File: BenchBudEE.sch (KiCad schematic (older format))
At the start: 0 parts

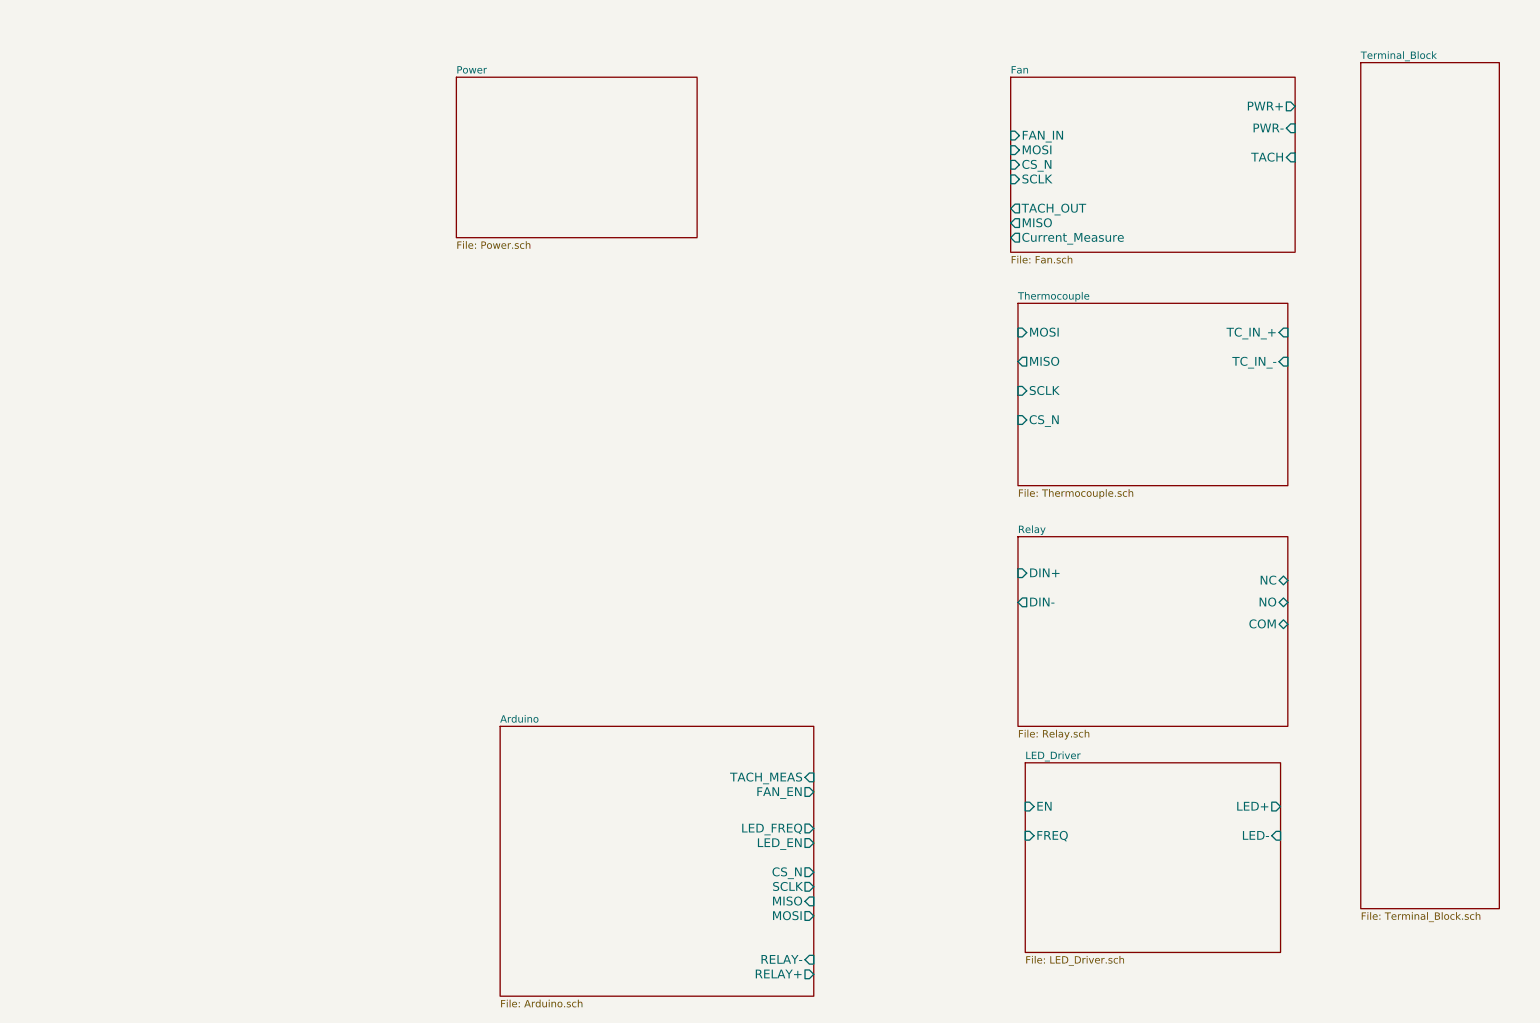
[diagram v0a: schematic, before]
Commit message: Created the first schematic in both Power modules
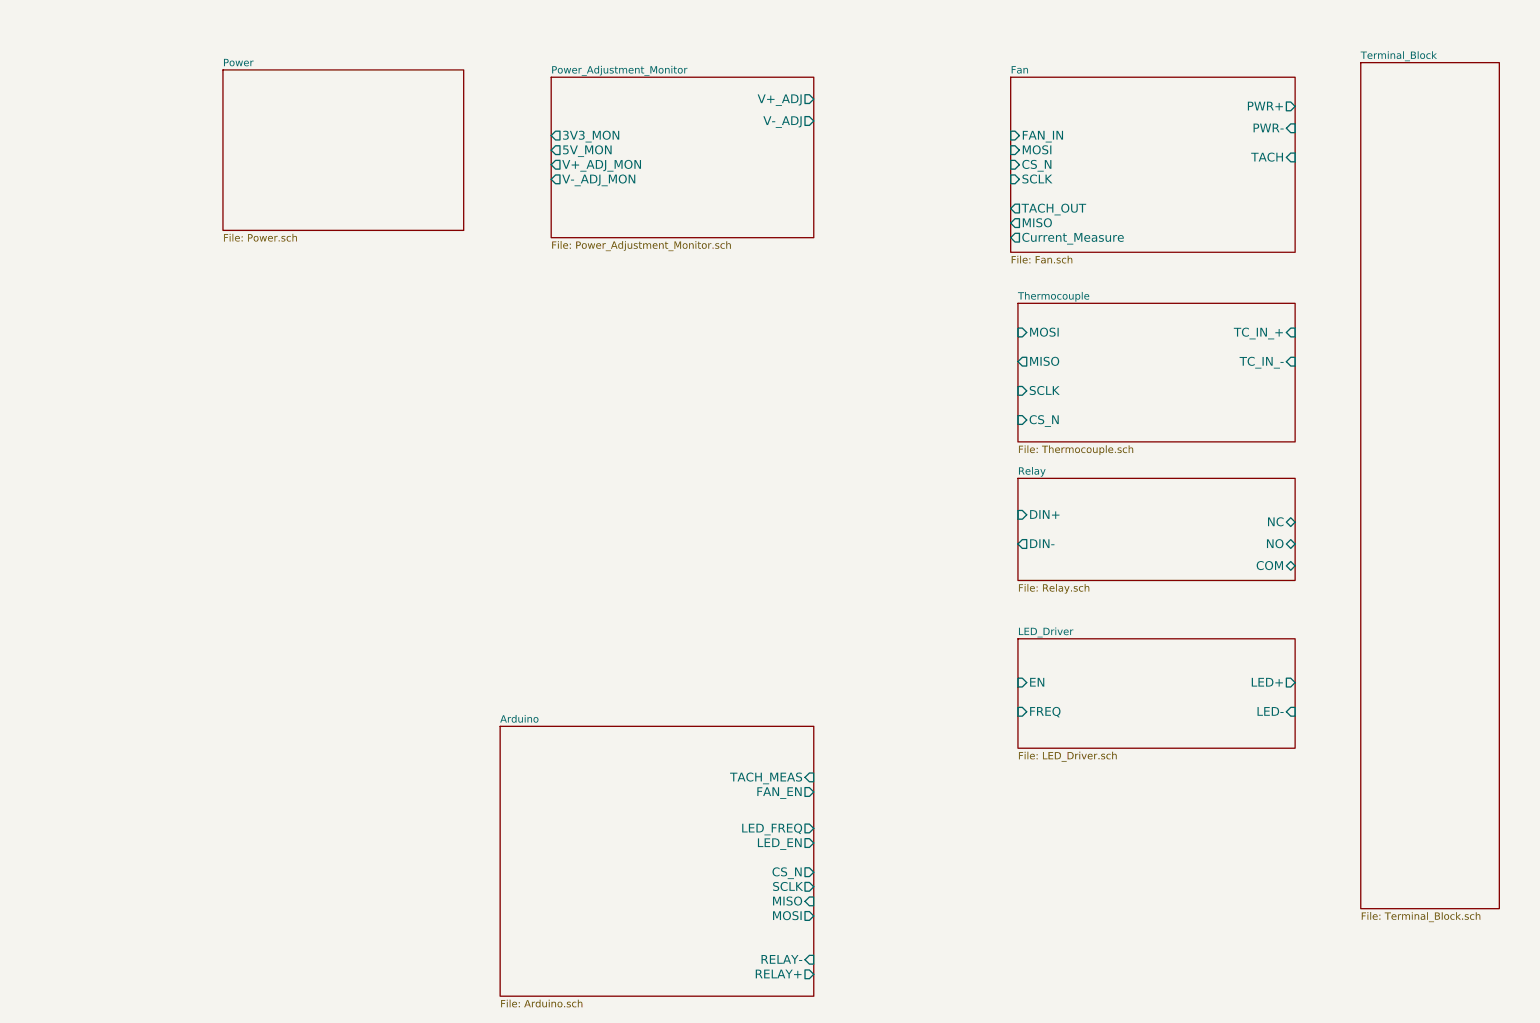
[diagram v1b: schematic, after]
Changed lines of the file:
@@
 $Descr A4 11693 8268
 encoding utf-8
-Sheet 1 8
+Sheet 1 9
 Title ""
-Date "9 feb 2014"
+Date "10 feb 2014"
 Rev ""
 Comp ""
@@
 $EndSheet
 $Sheet
-S 7550 2550 1850 1250
+S 7550 2550 1900 950
 U 52EE0AFF
 F0 "Thermocouple" 50
 F1 "Thermocouple.sch" 50
-F2 "TC_IN_+" I R 9400 2750 60
-F3 "TC_IN_-" I R 9400 2950 60
+F2 "TC_IN_+" I R 9450 2750 60
+F3 "TC_IN_-" I R 9450 2950 60
 F4 "MOSI" I L 7550 2750 60
 F5 "MISO" O L 7550 2950 60
@@
 $EndSheet
 $Sheet
-S 3700 1000 1650 1100
+S 2100 950  1650 1100
 U 52EE0B23
 F0 "Power" 50
@@
 $EndSheet
 $Sheet
-S 7600 5700 1750 1300
+S 7550 4850 1900 750
 U 52EE0B45
 F0 "LED_Driver" 50
 F1 "LED_Driver.sch" 50
-F2 "EN" I L 7600 6000 60
-F3 "FREQ" I L 7600 6200 60
-F4 "LED+" O R 9350 6000 60
-F5 "LED-" I R 9350 6200 60
+F2 "EN" I L 7550 5150 60
+F3 "FREQ" I L 7550 5350 60
+F4 "LED+" O R 9450 5150 60
+F5 "LED-" I R 9450 5350 60
 $EndSheet
 $Sheet
@@
 $EndSheet
 $Sheet
-S 7550 4150 1850 1300
+S 7550 3750 1900 700
 U 52EE0B15
 F0 "Relay" 50
 F1 "Relay.sch" 50
-F2 "DIN+" I L 7550 4400 60
-F3 "DIN-" O L 7550 4600 60
-F4 "NC" B R 9400 4450 60
-F5 "NO" B R 9400 4600 60
-F6 "COM" B R 9400 4750 60
+F2 "DIN+" I L 7550 4000 60
+F3 "DIN-" O L 7550 4200 60
+F4 "NC" B R 9450 4050 60
+F5 "NO" B R 9450 4200 60
+F6 "COM" B R 9450 4350 60
+$EndSheet
+$Sheet
+S 4350 1000 1800 1100
+U 52F76568
+F0 "Power_Adjustment_Monitor" 50
+F1 "Power_Adjustment_Monitor.sch" 50
+F2 "V+_ADJ" O R 6150 1150 60
+F3 "V-_ADJ" O R 6150 1300 60
+F4 "3V3_MON" O L 4350 1400 60
+F5 "5V_MON" O L 4350 1500 60
+F6 "V+_ADJ_MON" O L 4350 1600 60
+F7 "V-_ADJ_MON" O L 4350 1700 60
 $EndSheet
 $EndSCHEMATC

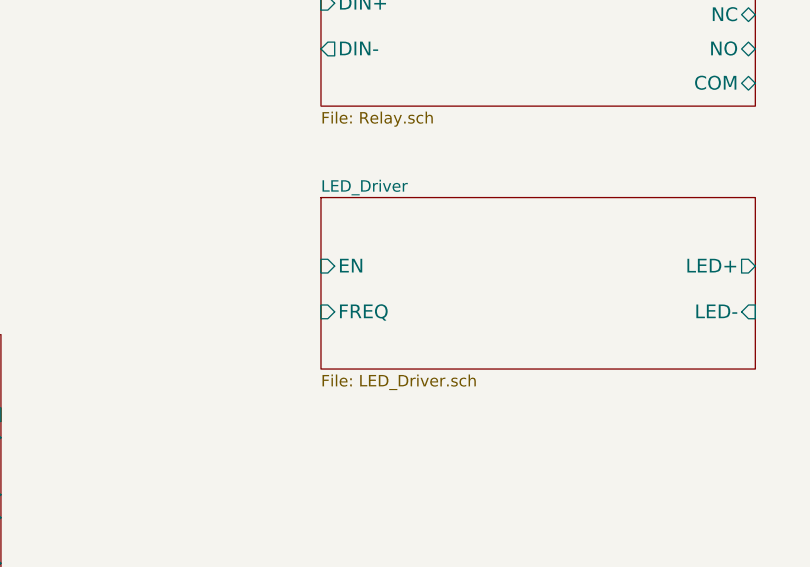
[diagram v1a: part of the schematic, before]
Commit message: Created first schematic for LED module
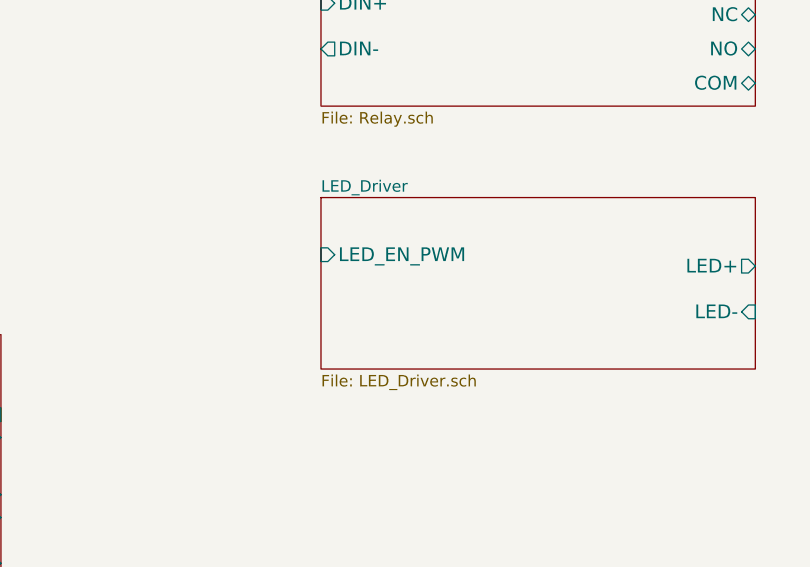
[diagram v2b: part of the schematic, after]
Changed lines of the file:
@@
 F0 "LED_Driver" 50
 F1 "LED_Driver.sch" 50
-F2 "EN" I L 7550 5150 60
-F3 "FREQ" I L 7550 5350 60
-F4 "LED+" O R 9450 5150 60
-F5 "LED-" I R 9450 5350 60
+F2 "LED+" O R 9450 5150 60
+F3 "LED-" I R 9450 5350 60
+F4 "LED_EN_PWM" I L 7550 5100 60
 $EndSheet
 $Sheet

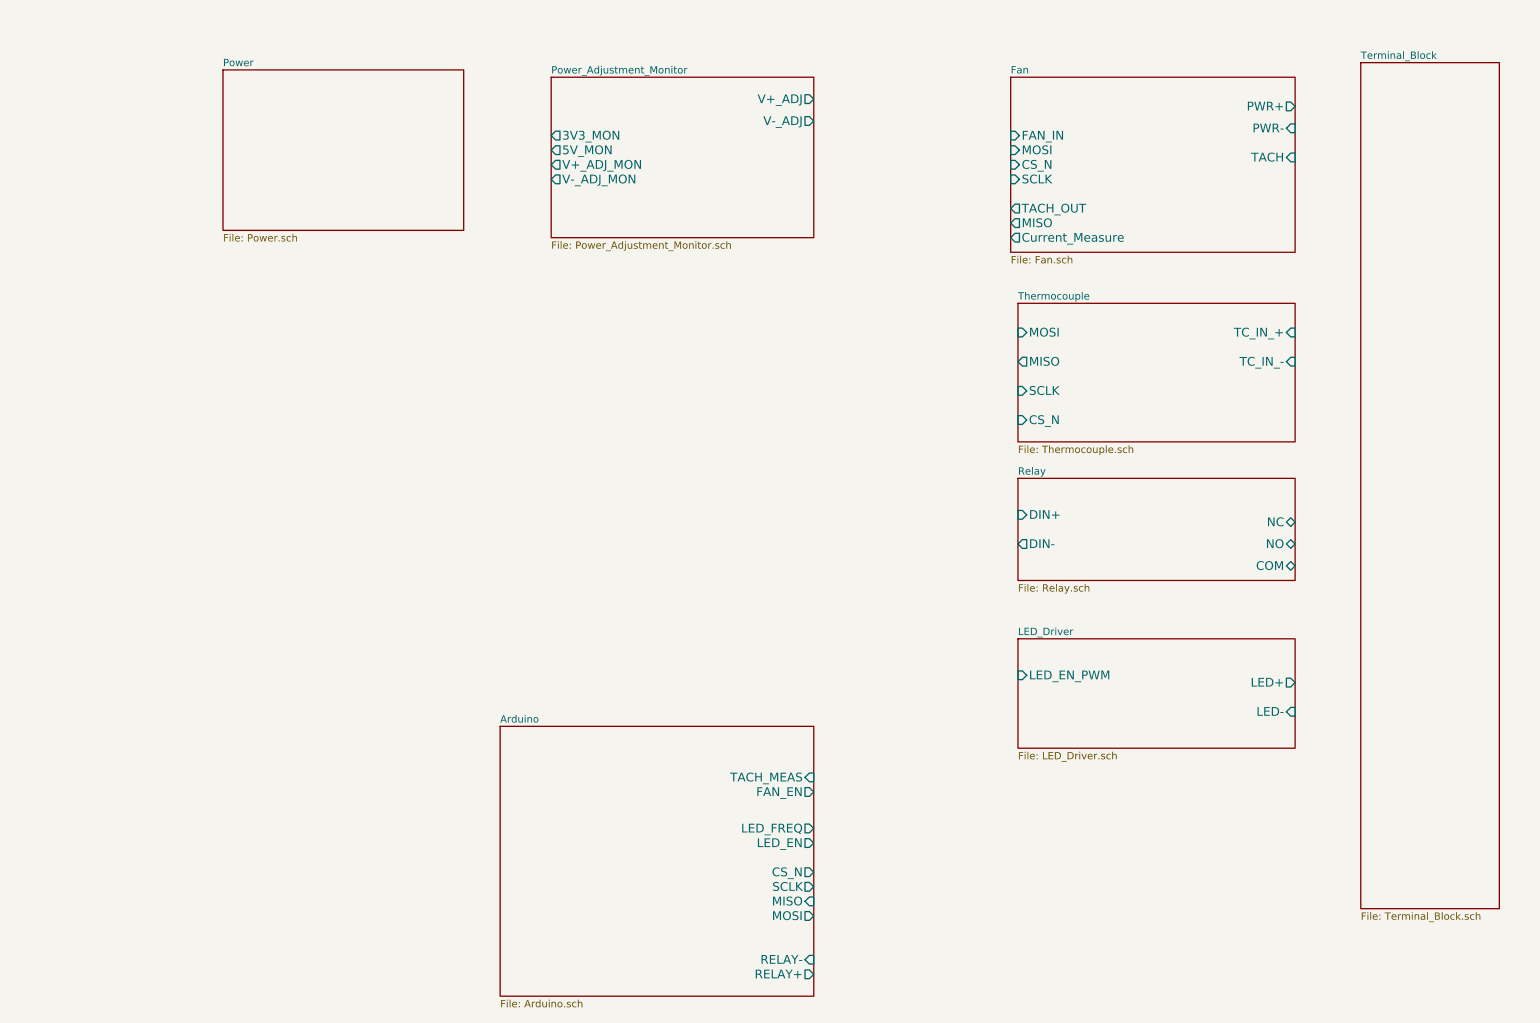
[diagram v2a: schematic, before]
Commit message: Created the Arduino module and then connected all the modules in the main schematic
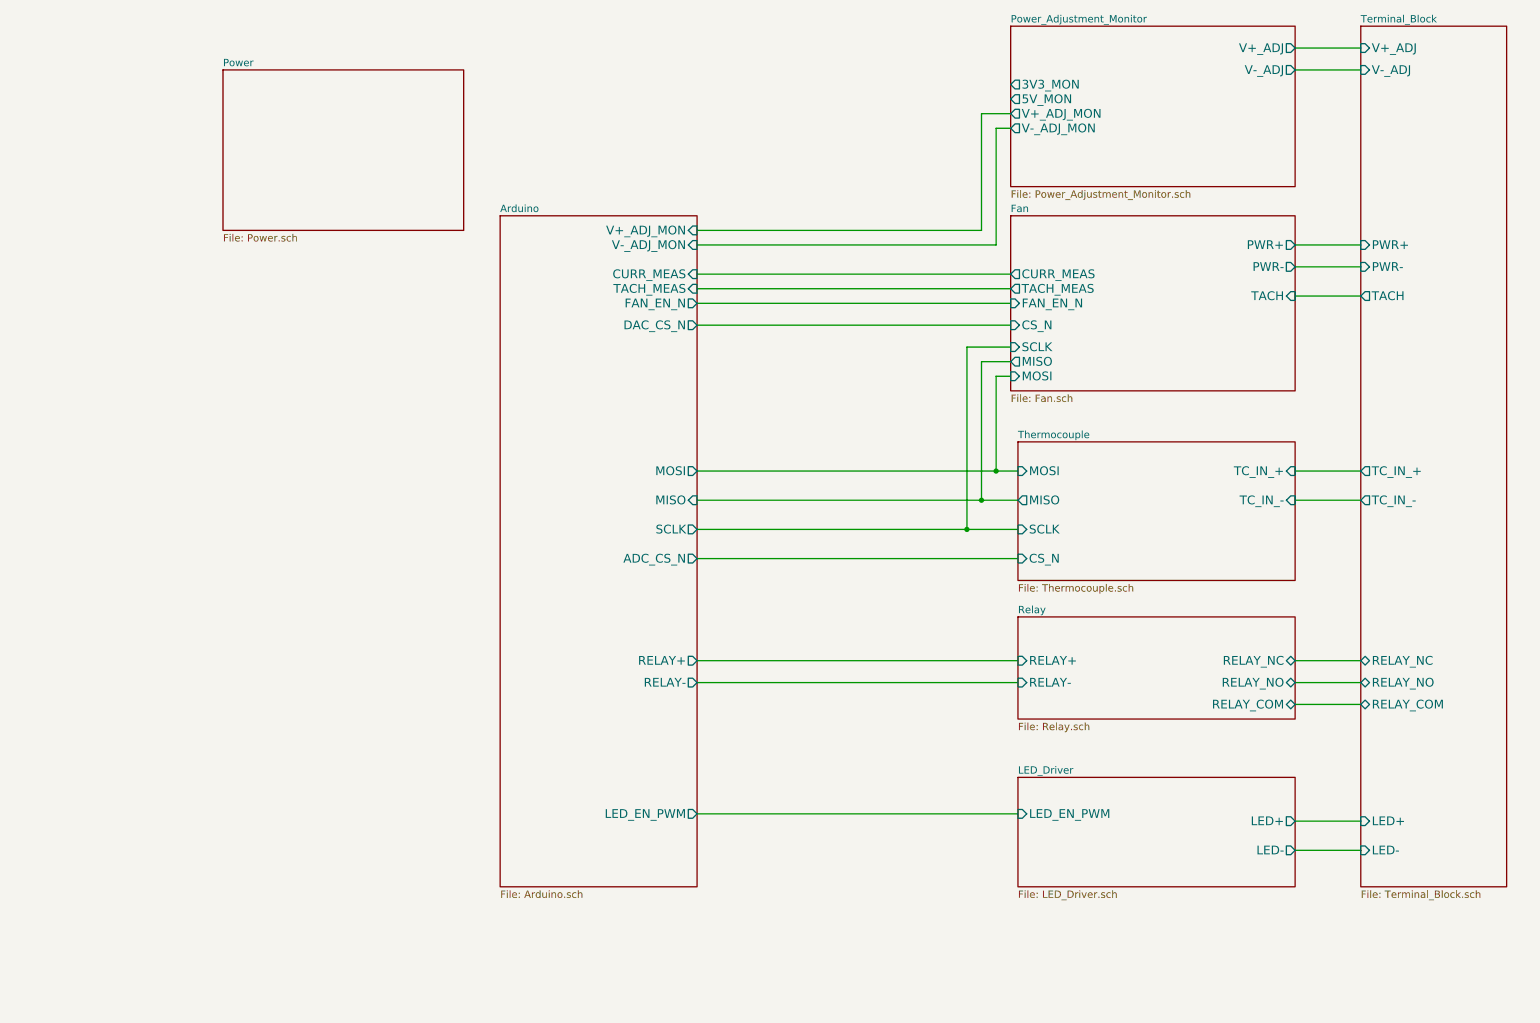
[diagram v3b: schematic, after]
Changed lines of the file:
@@
 $EndDescr
 $Sheet
-S 4000 5450 2150 1850
+S 4000 1950 1350 4600
 U 52EE0AAE
 F0 "Arduino" 50
 F1 "Arduino.sch" 50
-F2 "RELAY+" O R 6150 7150 60
-F3 "RELAY-" I R 6150 7050 60
-F4 "MOSI" O R 6150 6750 60
-F5 "MISO" I R 6150 6650 60
-F6 "SCLK" O R 6150 6550 60
-F7 "CS_N" O R 6150 6450 60
-F8 "LED_EN" O R 6150 6250 60
-F9 "LED_FREQ" O R 6150 6150 60
-F10 "FAN_EN" O R 6150 5900 60
-F11 "TACH_MEAS" I R 6150 5800 60
+F2 "MOSI" O R 5350 3700 60
+F3 "MISO" I R 5350 3900 60
+F4 "SCLK" O R 5350 4100 60
+F5 "TACH_MEAS" I R 5350 2450 60
+F6 "FAN_EN_N" O R 5350 2550 60
+F7 "CURR_MEAS" I R 5350 2350 60
+F8 "RELAY+" O R 5350 5000 60
+F9 "RELAY-" O R 5350 5150 60
+F10 "LED_EN_PWM" O R 5350 6050 60
+F11 "V+_ADJ_MON" I R 5350 2050 60
+F12 "V-_ADJ_MON" I R 5350 2150 60
+F13 "DAC_CS_N" O R 5350 2700 60
+F14 "ADC_CS_N" O R 5350 4300 60
 $EndSheet
 $Sheet
-S 7550 2550 1900 950
+S 7550 3500 1900 950
 U 52EE0AFF
 F0 "Thermocouple" 50
 F1 "Thermocouple.sch" 50
-F2 "TC_IN_+" I R 9450 2750 60
-F3 "TC_IN_-" I R 9450 2950 60
-F4 "MOSI" I L 7550 2750 60
-F5 "MISO" O L 7550 2950 60
-F6 "SCLK" I L 7550 3150 60
-F7 "CS_N" I L 7550 3350 60
+F2 "TC_IN_+" I R 9450 3700 60
+F3 "TC_IN_-" I R 9450 3900 60
+F4 "MOSI" I L 7550 3700 60
+F5 "MISO" O L 7550 3900 60
+F6 "SCLK" I L 7550 4100 60
+F7 "CS_N" I L 7550 4300 60
 $EndSheet
 $Sheet
@@
 $EndSheet
 $Sheet
-S 7550 4850 1900 750
+S 7550 5800 1900 750
 U 52EE0B45
 F0 "LED_Driver" 50
 F1 "LED_Driver.sch" 50
-F2 "LED+" O R 9450 5150 60
-F3 "LED-" I R 9450 5350 60
-F4 "LED_EN_PWM" I L 7550 5100 60
+F2 "LED+" O R 9450 6100 60
+F3 "LED_EN_PWM" I L 7550 6050 60
+F4 "LED-" O R 9450 6300 60
 $EndSheet
 $Sheet
-S 7500 1000 1950 1200
+S 7500 1950 1950 1200
 U 52EE0B67
 F0 "Fan" 50
 F1 "Fan.sch" 50
-F2 "PWR+" O R 9450 1200 60
-F3 "PWR-" I R 9450 1350 60
-F4 "TACH_OUT" O L 7500 1900 60
-F5 "FAN_IN" I L 7500 1400 60
-F6 "TACH" I R 9450 1550 60
-F7 "Current_Measure" O L 7500 2100 60
-F8 "MOSI" I L 7500 1500 60
-F9 "MISO" O L 7500 2000 60
-F10 "CS_N" I L 7500 1600 60
-F11 "SCLK" I L 7500 1700 60
+F2 "PWR+" O R 9450 2150 60
+F3 "TACH" I R 9450 2500 60
+F4 "MOSI" I L 7500 3050 60
+F5 "MISO" O L 7500 2950 60
+F6 "CS_N" I L 7500 2700 60
+F7 "SCLK" I L 7500 2850 60
+F8 "TACH_MEAS" O L 7500 2450 60
+F9 "CURR_MEAS" O L 7500 2350 60
+F10 "FAN_EN_N" I L 7500 2550 60
+F11 "PWR-" O R 9450 2300 60
 $EndSheet
 $Sheet
-S 9900 900  950  5800
+S 7550 4700 1900 700
+U 52EE0B15
+F0 "Relay" 50
+F1 "Relay.sch" 50
+F2 "RELAY_NC" B R 9450 5000 60
+F3 "RELAY_NO" B R 9450 5150 60
+F4 "RELAY_COM" B R 9450 5300 60
+F5 "RELAY+" I L 7550 5000 60
+F6 "RELAY-" I L 7550 5150 60
+$EndSheet
+$Sheet
+S 7500 650  1950 1100
+U 52F76568
+F0 "Power_Adjustment_Monitor" 50
+F1 "Power_Adjustment_Monitor.sch" 50
+F2 "V+_ADJ" O R 9450 800 60
+F3 "V-_ADJ" O R 9450 950 60
+F4 "3V3_MON" O L 7500 1050 60
+F5 "5V_MON" O L 7500 1150 60
+F6 "V+_ADJ_MON" O L 7500 1250 60
+F7 "V-_ADJ_MON" O L 7500 1350 60
+$EndSheet
+$Sheet
+S 9900 650  1000 5900
 U 52EE0B92
 F0 "Terminal_Block" 50
 F1 "Terminal_Block.sch" 50
+F2 "V+_ADJ" I L 9900 800 60
+F3 "V-_ADJ" I L 9900 950 60
+F4 "PWR+" I L 9900 2150 60
+F5 "PWR-" I L 9900 2300 60
+F6 "TACH" O L 9900 2500 60
+F7 "TC_IN_+" O L 9900 3700 60
+F8 "TC_IN_-" O L 9900 3900 60
+F9 "LED+" I L 9900 6100 60
+F10 "LED-" I L 9900 6300 60
+F11 "RELAY_NC" B L 9900 5000 60
+F12 "RELAY_NO" B L 9900 5150 60
+F13 "RELAY_COM" B L 9900 5300 60
 $EndSheet
-$Sheet
-S 7550 3750 1900 700
-U 52EE0B15
-F0 "Relay" 50
-F1 "Relay.sch" 50
-F2 "DIN+" I L 7550 4000 60
-F3 "DIN-" O L 7550 4200 60
-F4 "NC" B R 9450 4050 60
-F5 "NO" B R 9450 4200 60
-F6 "COM" B R 9450 4350 60
-$EndSheet
-$Sheet
-S 4350 1000 1800 1100
-U 52F76568
-F0 "Power_Adjustment_Monitor" 50
-F1 "Power_Adjustment_Monitor.sch" 50
-F2 "V+_ADJ" O R 6150 1150 60
-F3 "V-_ADJ" O R 6150 1300 60
-F4 "3V3_MON" O L 4350 1400 60
-F5 "5V_MON" O L 4350 1500 60
-F6 "V+_ADJ_MON" O L 4350 1600 60
-F7 "V-_ADJ_MON" O L 4350 1700 60
-$EndSheet
+Wire Wire Line
+	9450 800  9900 800
+Wire Wire Line
+	9450 950  9900 950
+Wire Wire Line
+	9450 2150 9900 2150
+Wire Wire Line
+	9450 2300 9900 2300
+Wire Wire Line
+	9450 2500 9900 2500
+Wire Wire Line
+	9450 3700 9900 3700
+Wire Wire Line
+	9450 3900 9900 3900
+Wire Wire Line
+	9450 5000 9900 5000
+Wire Wire Line
+	9450 5150 9900 5150
+Wire Wire Line
+	9450 5300 9900 5300
+Wire Wire Line
+	9450 6100 9900 6100
+Wire Wire Line
+	9450 6300 9900 6300
+Wire Wire Line
+	5350 5000 7550 5000
+Wire Wire Line
+	5350 5150 7550 5150
+Wire Wire Line
+	5350 3700 7550 3700
+Wire Wire Line
+	5350 3900 7550 3900
+Wire Wire Line
+	5350 4100 7550 4100
+Wire Wire Line
+	7500 3050 7400 3050
+Wire Wire Line
+	7400 3050 7400 3700
+Connection ~ 7400 3700
+Wire Wire Line
+	7500 2950 7300 2950
+Wire Wire Line
+	7300 2950 7300 3900
+Connection ~ 7300 3900
+Wire Wire Line
+	7500 2850 7200 2850
+Wire Wire Line
+	7200 2850 7200 4100
+Connection ~ 7200 4100
+Wire Wire Line
+	7550 6050 5350 6050
+Wire Wire Line
+	5350 2550 7500 2550
+Wire Wire Line
+	7500 2450 5350 2450
+Wire Wire Line
+	5350 2350 7500 2350
+Wire Wire Line
+	5350 2050 7300 2050
+Wire Wire Line
+	7300 2050 7300 1250
+Wire Wire Line
+	7300 1250 7500 1250
+Wire Wire Line
+	5350 2150 7400 2150
+Wire Wire Line
+	7400 2150 7400 1350
+Wire Wire Line
+	7400 1350 7500 1350
+Wire Wire Line
+	5350 2700 7500 2700
+Wire Wire Line
+	5350 4300 7550 4300
 $EndSCHEMATC
